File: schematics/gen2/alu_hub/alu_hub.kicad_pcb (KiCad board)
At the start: 2 copper layers, 100 x 91.1 mm, 22 parts, among them U1 74LS574, U10 74LS02, U2 74LS245, U3 74LS02, U4 74LS181, U5 74LS181, U6 74LS574, U7 74LS245, U8 74LS245, U9 74LS02

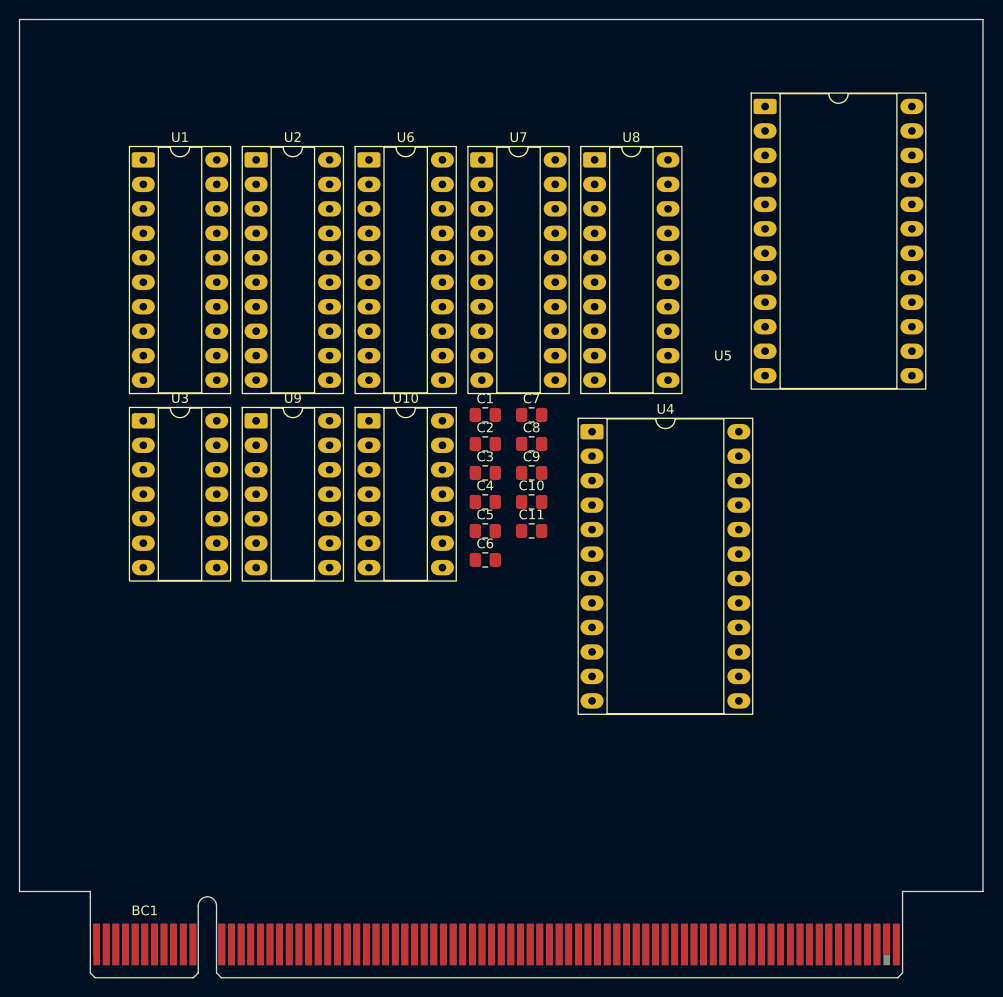
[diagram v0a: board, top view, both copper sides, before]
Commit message: feat: position files path in ALU Hub schematic configuration
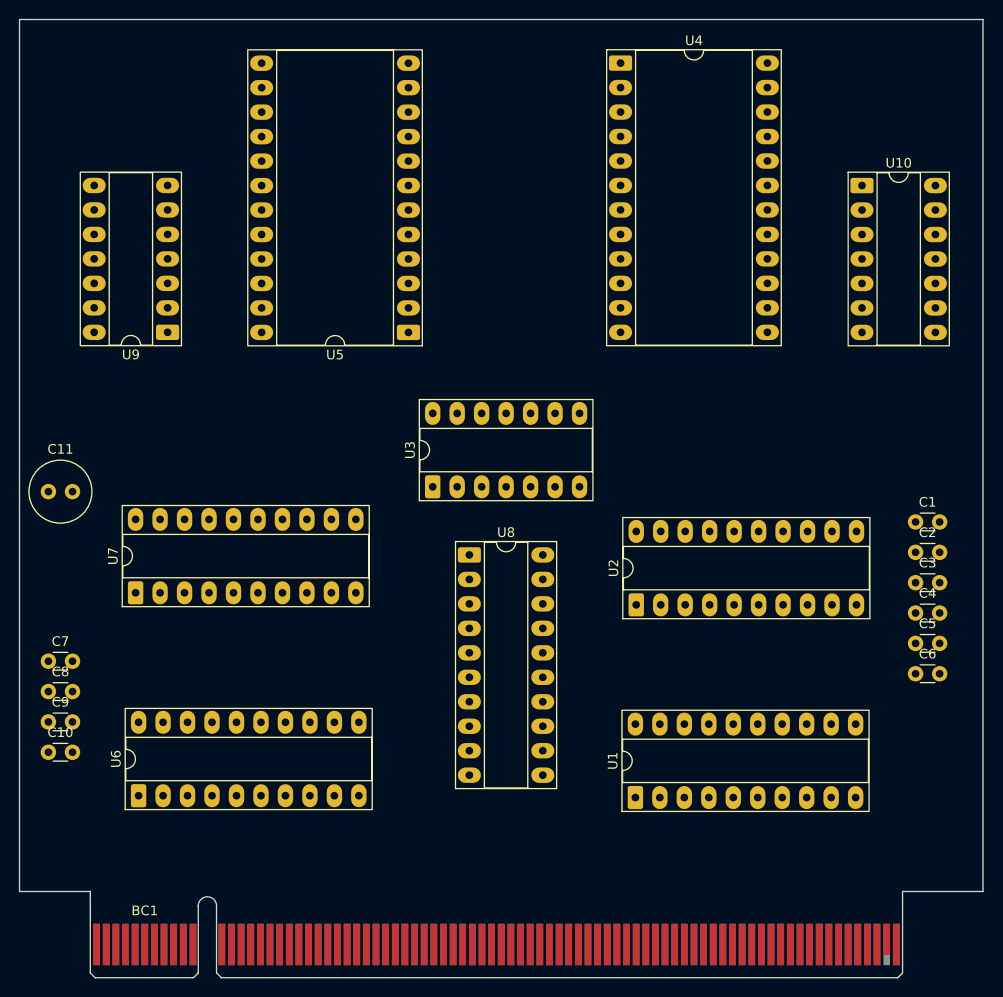
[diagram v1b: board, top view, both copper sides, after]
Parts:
- C1, C10, C2, C3, C4, C5, C6, C7, C8, C9: footprint Capacitor_SMD:C_0805_2012Metric_Pad1.18x1.45mm_HandSolder -> Capacitor_THT:C_Disc_D3.0mm_W1.6mm_P2.50mm
- C11: footprint Capacitor_SMD:C_0805_2012Metric_Pad1.18x1.45mm_HandSolder -> Capacitor_THT:C_Radial_D6.3mm_H5.0mm_P2.50mm
- moved U1 83.6 mm to (163.9, 125.2), turned to 90 degrees
- moved U6 70.2 mm to (112.4, 125.1), turned to 90 degrees
- moved U2 60.7 mm to (164.0, 105.2), turned to 90 degrees
- moved U7 57.5 mm to (112.0, 104.0), turned to 90 degrees
- moved U10 56.7 mm to (187.4, 61.7)
- moved C10 56.5 mm to (103.0, 120.5)
- moved C9 56.4 mm to (103.0, 117.4)
- moved C8 56.4 mm to (103.0, 114.2)
- moved C7 56.3 mm to (103.0, 111.1)
- moved C11 50.3 mm to (103.0, 93.5)
- moved C6 46.2 mm to (193.0, 112.4)
- moved C5 46.2 mm to (193.0, 109.2)
- moved C4 46.1 mm to (193.0, 106.1)
- moved C3 46.1 mm to (193.0, 103.0)
- moved C2 46.1 mm to (193.0, 99.8)
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
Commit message: feat(alu): added vcc and gnd back plate
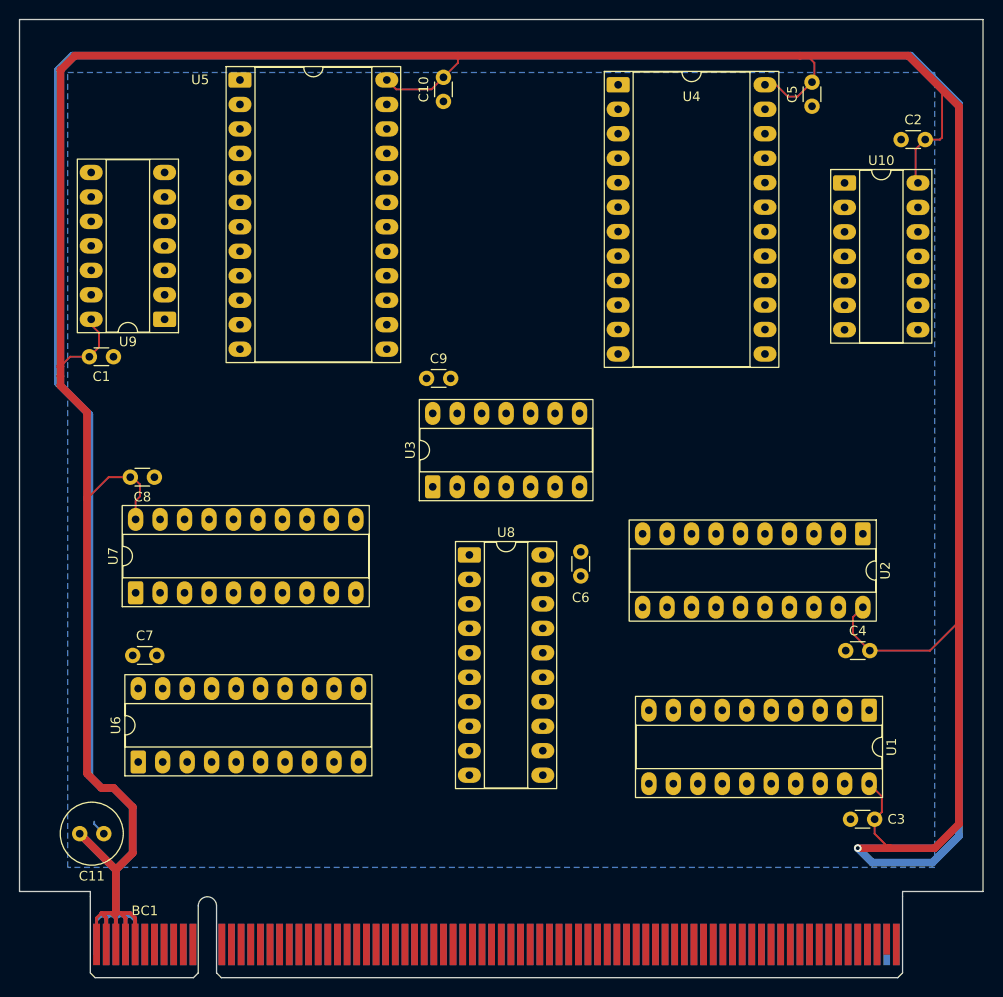
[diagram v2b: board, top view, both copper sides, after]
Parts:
- moved C1 85.0 mm to (109.8, 79.5), turned to 180 degrees
- moved C10 79.0 mm to (144.0, 53.0), turned to 90 degrees
- moved C5 56.8 mm to (182.2, 53.5), turned to 90 degrees
- moved C9 53.0 mm to (142.2, 81.8)
- moved C2 42.9 mm to (191.5, 57.0)
- moved C6 36.2 mm to (158.2, 102.2), turned to 90 degrees
- moved C11 36.0 mm to (108.8, 129.0), turned to 180 degrees
- moved U5 31.5 mm to (122.9, 50.8), turned to 0 degrees
- moved U1 25.9 mm to (188.2, 116.2), turned to -90 degrees
- moved C3 25.5 mm to (186.2, 127.5)
- moved C8 24.8 mm to (114.0, 92.0), turned to 180 degrees
- moved U2 24.6 mm to (187.5, 97.9), turned to -90 degrees
- moved C7 8.77 mm to (111.8, 110.5)
- moved C4 8.23 mm to (185.8, 110.0)
- moved U6 3.50 mm to (112.3, 121.6)
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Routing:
- net VCC: track 0.00 -> 674.4 mm, vias 0 -> 1
- net GND: track 0.00 -> 1.66 mm
- added copper zone on B.Cu, net GND

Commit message: feat: added gnd connections for alu hub
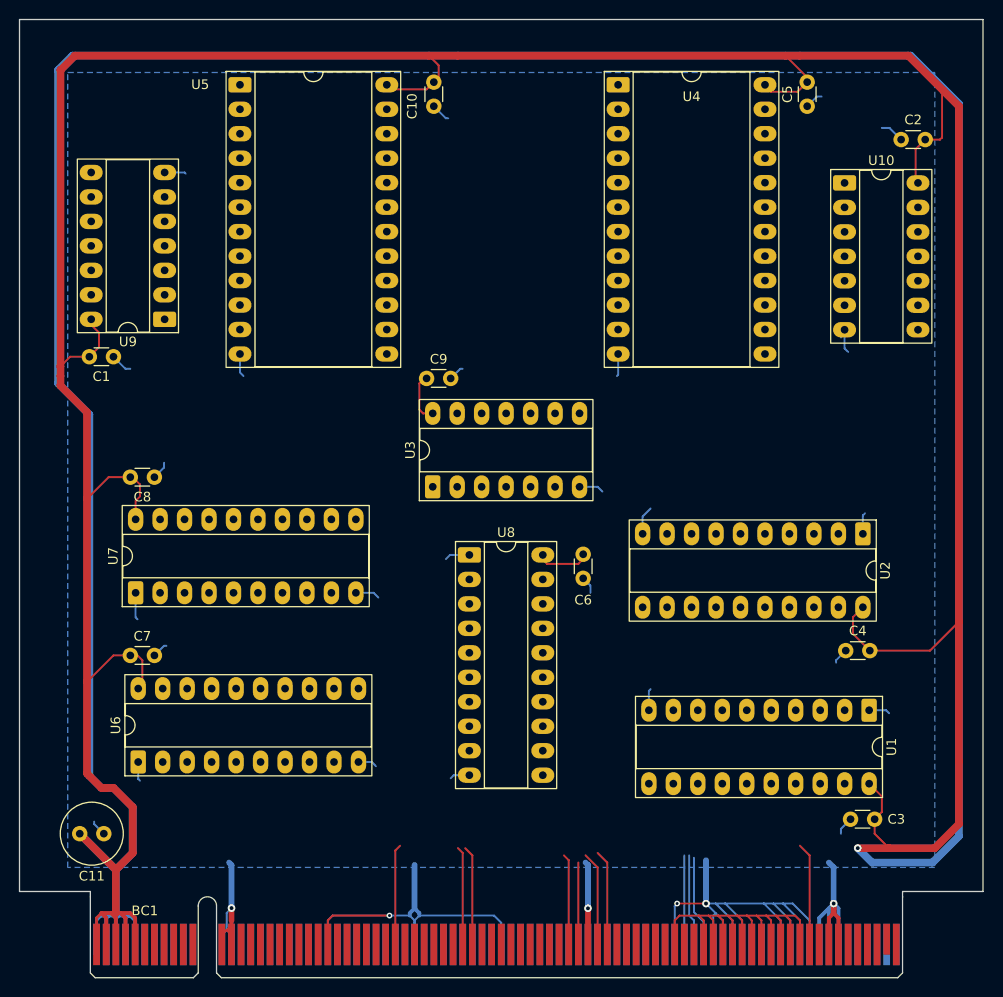
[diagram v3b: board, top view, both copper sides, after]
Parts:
- moved C9 2.50 mm to (144.8, 81.8), turned to 180 degrees
- moved C7 2.25 mm to (114.0, 110.5), turned to 180 degrees
- moved C10 1.12 mm to (143.0, 53.5)
- moved C5 0.50 mm to (181.8, 53.5)
- moved U5 0.50 mm to (122.9, 51.3)
- moved C6 0.35 mm to (158.5, 102.5)
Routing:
- net GND: track 1.66 -> 259.8 mm, vias 0 -> 6
- net VCC: track 674.4 -> 693.8 mm
- net Net-(BC1-~{CLK}): track 0.00 -> 10.7 mm
- net Net-(BC1-~{RALU}): track 0.00 -> 10.5 mm
- net Net-(BC1-~{ALUCI}): track 0.00 -> 10.3 mm
- net Net-(BC1-ALUM): track 0.00 -> 10.2 mm
- net Net-(BC1-ALUS3): track 0.00 -> 9.91 mm
- net Net-(BC1-ALUS2): track 0.00 -> 9.77 mm
- net Net-(BC1-~{ALUCO}): track 0.00 -> 9.46 mm
- net Net-(BC1-ALUS0): track 0.00 -> 9.46 mm
- net Net-(BC1-ALUSO): track 0.00 -> 9.41 mm
- net Net-(BC1-ALUZO): track 0.00 -> 9.25 mm
- net Net-(BC1-ALUS1): track 0.00 -> 8.50 mm

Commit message: fix: gnd plate
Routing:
- net VCC: track 693.8 -> 421.6 mm
- net GND: track 259.8 -> 508.6 mm

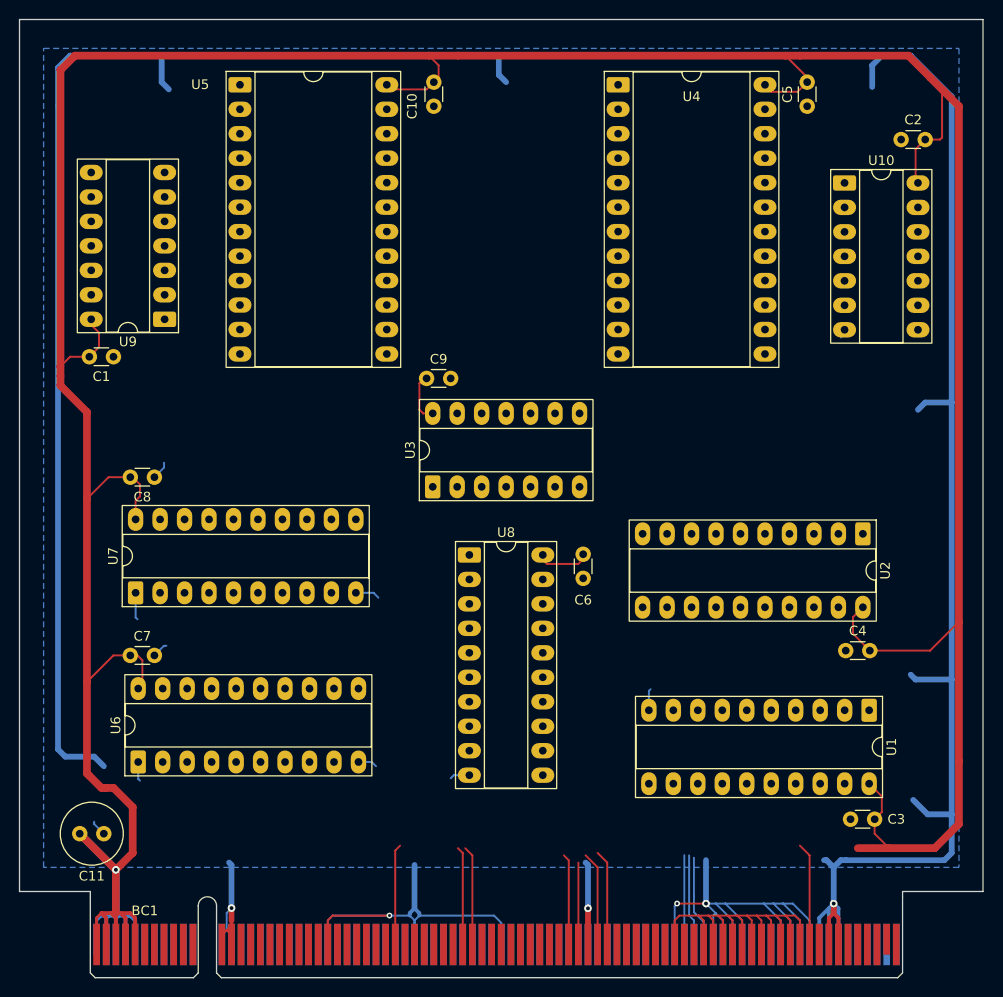
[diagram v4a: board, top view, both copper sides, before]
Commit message: fix: changed the placement
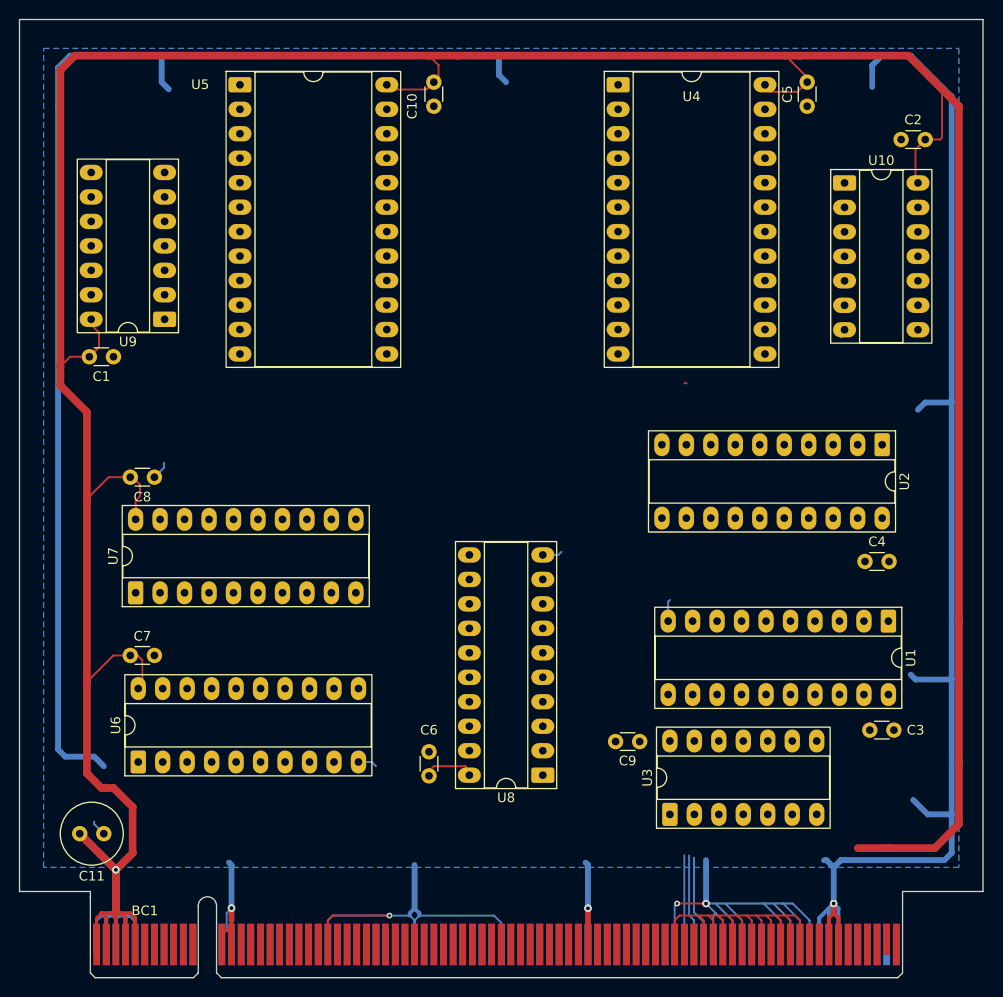
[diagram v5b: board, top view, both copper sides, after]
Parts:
- moved U3 42.0 mm to (167.5, 127.0)
- moved C9 41.4 mm to (161.9, 119.4), turned to 0 degrees
- moved U8 24.1 mm to (154.3, 122.9), turned to 180 degrees
- moved C6 24.1 mm to (142.5, 120.5), turned to -90 degrees
- moved C3 9.46 mm to (188.2, 118.2)
- moved C4 9.46 mm to (187.8, 100.8)
- moved U1 9.46 mm to (190.2, 106.9)
- moved U2 9.46 mm to (189.5, 88.6)
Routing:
- net VCC: track 421.6 -> 392.3 mm
- net Net-(BC1-~{CLK}): track 10.7 -> 0.00 mm
- net Net-(BC1-~{RALU}): track 10.5 -> 0.00 mm
- net Net-(BC1-~{ALUCI}): track 10.3 -> 0.00 mm
- net Net-(BC1-ALUM): track 10.2 -> 0.00 mm
- net Net-(BC1-ALUS3): track 9.91 -> 0.00 mm
- net Net-(BC1-ALUS2): track 9.77 -> 0.00 mm
- net Net-(BC1-ALUS0): track 9.46 -> 0.00 mm
- net GND: track 508.6 -> 499.5 mm
- net Net-(BC1-ALUS1): track 8.50 -> 0.00 mm

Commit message: feat: alu hub
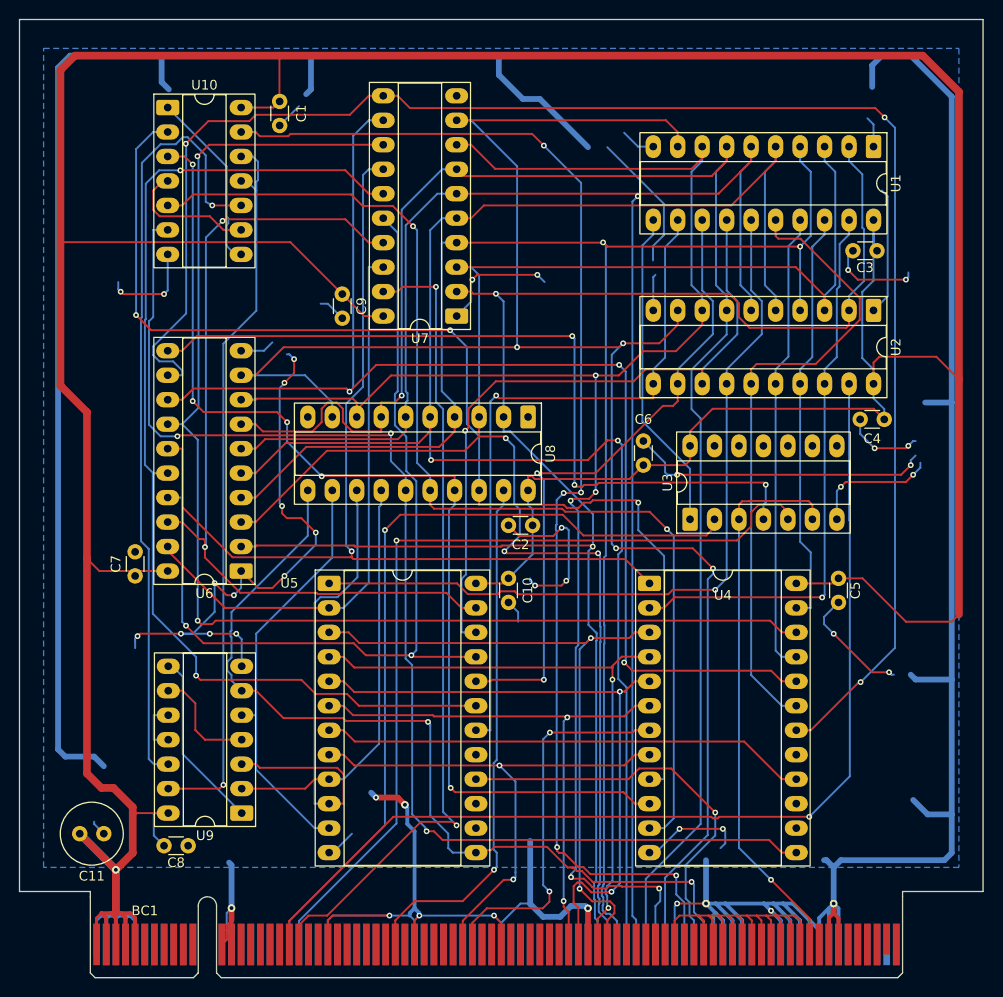
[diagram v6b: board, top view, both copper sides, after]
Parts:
- moved U10 70.7 mm to (115.4, 53.6)
- moved C2 57.1 mm to (150.8, 97.0)
- moved U5 52.6 mm to (132.1, 103.0)
- moved C9 52.3 mm to (133.5, 75.5), turned to 90 degrees
- moved C10 52.1 mm to (150.8, 105.0)
- moved U9 51.9 mm to (123.1, 126.9)
- moved U4 51.9 mm to (165.4, 103.0)
- moved C5 51.6 mm to (185.0, 105.0)
- moved C3 49.8 mm to (186.5, 68.5)
- moved U1 49.3 mm to (188.6, 57.7)
- moved U7 44.0 mm to (145.4, 75.3), turned to 180 degrees
- moved C6 39.2 mm to (164.8, 88.2)
- moved C8 38.4 mm to (117.5, 130.2)
- moved U8 37.2 mm to (152.8, 85.8), turned to -90 degrees
- moved U3 30.7 mm to (169.6, 96.4)
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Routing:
- net GND: track 499.5 -> 783.2 mm, vias 6 -> 41
- net /DATA7: track 0.00 -> 187.1 mm, vias 0 -> 4
- net /DATA3: track 0.00 -> 178.3 mm, vias 0 -> 2
- net /DATA4: track 0.00 -> 175.7 mm, vias 0 -> 1
- net /DATA2: track 0.00 -> 174.6 mm, vias 0 -> 2
- net /LOW7: track 0.00 -> 173.8 mm, vias 0 -> 3
- net /DATA1: track 0.00 -> 173.6 mm, vias 0 -> 3
- net /DATA0: track 0.00 -> 172.7 mm, vias 0 -> 2
- net /DATA6: track 0.00 -> 171.7 mm, vias 0 -> 5
- net /DATA5: track 0.00 -> 169.6 mm, vias 0 -> 1
- net /LOW5: track 0.00 -> 133.8 mm, vias 0 -> 2
- net Net-(U4-F3): track 0.00 -> 129.8 mm, vias 0 -> 3
- net /LOW6: track 0.00 -> 129.0 mm, vias 0 -> 3
- net Net-(U4-F0): track 0.00 -> 122.3 mm, vias 0 -> 3
- net Net-(BC1-ALUZO): track 9.25 -> 130.1 mm, vias 0 -> 5
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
